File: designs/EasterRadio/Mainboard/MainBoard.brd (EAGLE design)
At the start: 236 x 57.5 mm, 84 parts, among them IC1 74HC595D, IC2 74HC595D, IC3 74HC595D, IC4 Analog Digital, IC6 CP2102, Q1 SS8050-G, Q2 SS8050-G

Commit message: checked Mainboard and esp32
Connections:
- net 3.3V: no longer GPIOS.5
- net CS2: now also GPIOS.5
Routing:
- net CS2: track 6.06 -> 45.0 mm, vias 0 -> 3
- net 3.3V: track 418.7 -> 421.2 mm
- net GND: track 55.9 -> 54.2 mm
- net SDA: track 202.4 -> 201.6 mm
- net RST_RADIO_IC: track 172.3 -> 171.7 mm

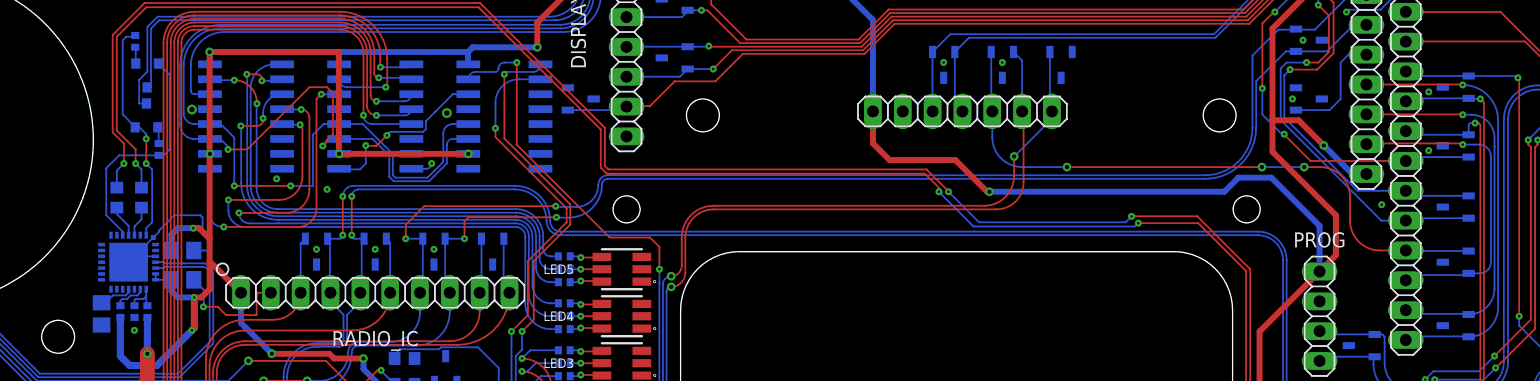
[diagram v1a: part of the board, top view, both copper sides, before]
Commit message: small change to flsh chip for esp32
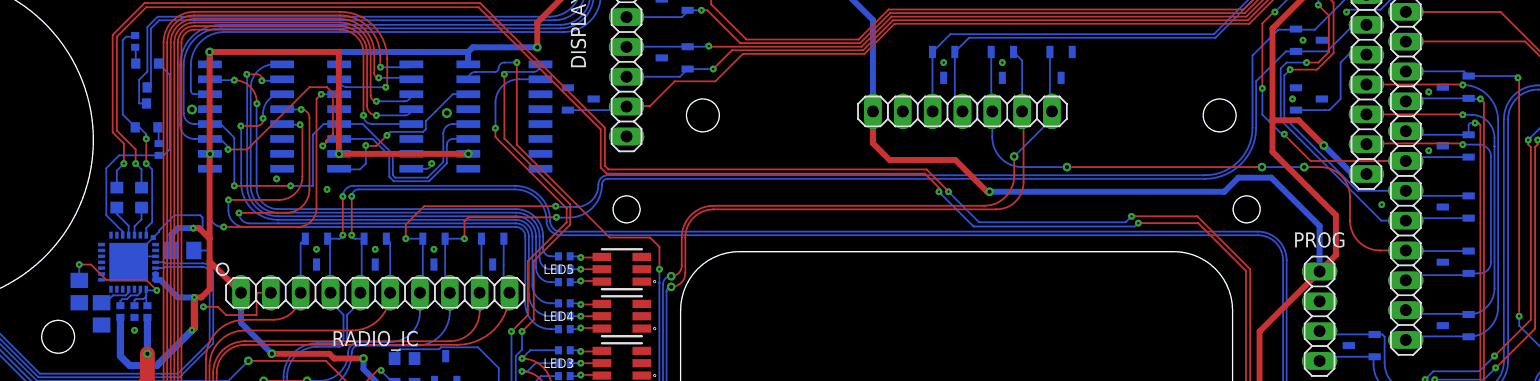
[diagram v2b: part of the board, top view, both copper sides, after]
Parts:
- removed C2: 0.1uF, rcl:C0805
- added C3: 1uF, rcl:C0805
- C1: value 4.7uF -> 10uF
- R20: value 10Kohm -> 1Kohm
- R21: value 2Kohm -> 10Kohm
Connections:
- net CS2 renamed IO34
- net 3.3V: no longer C2.1
- net GND: now also C3.1; no longer C2.2
- net N$44: now also C3.2
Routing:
- net N$44: track 3.05 -> 12.8 mm, vias 0 -> 2
- net GND: track 54.2 -> 51.6 mm
- net 3.3V: track 421.2 -> 420.7 mm
- net IO34: track 45.0 -> 44.5 mm
